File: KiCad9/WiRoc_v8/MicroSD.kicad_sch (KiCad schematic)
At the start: 13 parts, among them J3 Micro_SD_Card_Det1

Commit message: etc
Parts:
- J3: LCSC Part # (none) -> C2962372; Manufacturer (none) -> Hanbo Electronic; ManufacturerPartNumber (none) -> TF-018B-H15
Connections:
- net SDC0-CLK-2: now reaches J3.5 (CLK), R22.2, RV6.1
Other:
- moved on the sheet: R22
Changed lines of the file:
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@@
 	(wire
 		(pts
-			(xy 58.42 71.12) (xy 63.5 71.12)
+			(xy 53.34 71.12) (xy 60.96 71.12)
 		)
 		(stroke
@@
 	(wire
 		(pts
-			(xy 71.12 71.12) (xy 93.98 71.12)
+			(xy 68.58 71.12) (xy 93.98 71.12)
 		)
 		(stroke
@@
 			(width 0)
 			(type default)
+		)
+	)
+	(label "SDC0-CLK-2"
+		(at 90.17 71.12 0)
+		(effects
+			(font
+				(size 1.524 1.524)
+			)
+			(justify left bottom)
 		)
 	)
@@
 	(global_label "SDC0-CLK"
 		(shape input)
-		(at 58.42 71.12 180)
+		(at 53.34 71.12 180)
 		(fields_autoplaced yes)
 		(effects
@@
 		)
 		(property "Intersheetrefs" "${INTERSHEET_REFS}"
-			(at 43.5038 71.12 0)
+			(at 38.4238 71.12 0)
 			(effects
 				(font
@@
 				(justify right)
 				(hide yes)
+			)
+		)
+	)
+	(rule_area
+		(polyline
+			(pts
+				(xy 69.85 58.42) (xy 69.85 86.36) (xy 72.39 86.36) (xy 72.39 58.42)
+			)
+			(stroke
+				(width 0)
+				(type dash)
+			)
+			(fill
+				(type none)
+			)
+		)
+	)
+	(netclass_flag ""
+		(length 2.54)
+		(shape round)
+		(at 55.88 71.12 0)
+		(fields_autoplaced yes)
+		(effects
+			(font
+				(size 1.524 1.524)
+			)
+			(justify left bottom)
+		)
+		(property "Netclass" "SD-CARD-LINES"
+			(at 56.5099 68.58 0)
+			(effects
+				(font
+					(size 1.27 1.27)
+				)
+				(justify left)
+			)
+		)
+		(property "Component Class" ""
+			(at -130.81 35.56 0)
+			(effects
+				(font
+					(size 1.27 1.27)
+					(italic yes)
+				)
+			)
+		)
+	)
+	(netclass_flag ""
+		(length 2.54)
+		(shape round)
+		(at 71.12 58.42 0)
+		(fields_autoplaced yes)
+		(effects
+			(font
+				(size 1.524 1.524)
+			)
+			(justify left bottom)
+		)
+		(property "Netclass" "SD-CARD-LINES"
+			(at 71.7499 55.88 0)
+			(effects
+				(font
+					(size 1.27 1.27)
+				)
+				(justify left)
+			)
+		)
+		(property "Component Class" ""
+			(at -115.57 22.86 0)
+			(effects
+				(font
+					(size 1.27 1.27)
+					(italic yes)
+				)
 			)
 		)
@@
 			)
 		)
+		(property "LCSC Part #" "C2962372"
+			(at 148.59 71.12 0)
+			(effects
+				(font
+					(size 1.27 1.27)
+				)
+				(hide yes)
+			)
+		)
+		(property "Manufacturer" "Hanbo Electronic"
+			(at 148.59 71.12 0)
+			(effects
+				(font
+					(size 1.27 1.27)
+				)
+				(hide yes)
+			)
+		)
+		(property "ManufacturerPartNumber" "TF-018B-H15"
+			(at 148.59 71.12 0)
+			(effects
+				(font
+					(size 1.27 1.27)
+				)
+				(hide yes)
+			)
+		)
 		(pin "7"
 		)
@@
 	(symbol
 		(lib_id "Device:R")
-		(at 67.31 71.12 90)
+		(at 64.77 71.12 90)
 		(unit 1)
 		(exclude_from_sim no)
@@
 		(dnp no)
 		(property "Reference" "R22"
-			(at 72.39 73.66 90)
+			(at 69.85 73.66 90)
 			(effects
 				(font
@@
 		)
 		(property "Value" "33R"
-			(at 63.5 73.66 90)
+			(at 60.96 73.66 90)
 			(effects
 				(font
@@
 		)
 		(property "Footprint" "Resistor_SMD:R_0402_1005Metric"
-			(at 67.31 72.898 90)
+			(at 64.77 72.898 90)
 			(effects
 				(font
@@
 		)
 		(property "Datasheet" "~"
-			(at 67.31 71.12 0)
+			(at 64.77 71.12 0)
 			(effects
 				(font
@@
 		)
 		(property "Description" ""
-			(at 67.31 71.12 0)
-			(effects
-				(font
+			(at 64.77 71.12 0)
+			(effects
+				(font

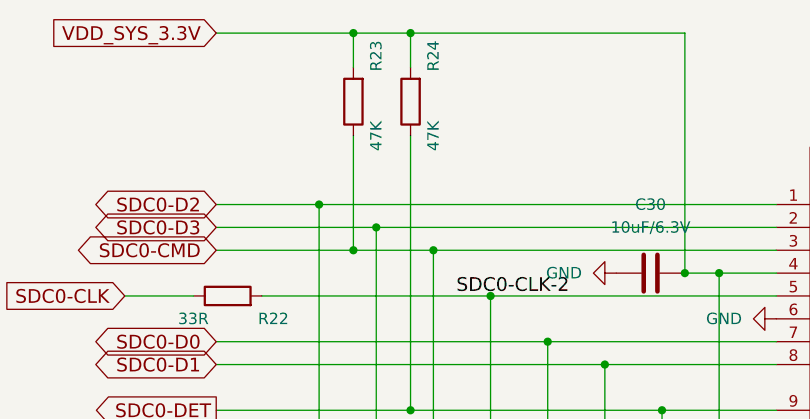
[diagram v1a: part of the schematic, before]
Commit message: add bom
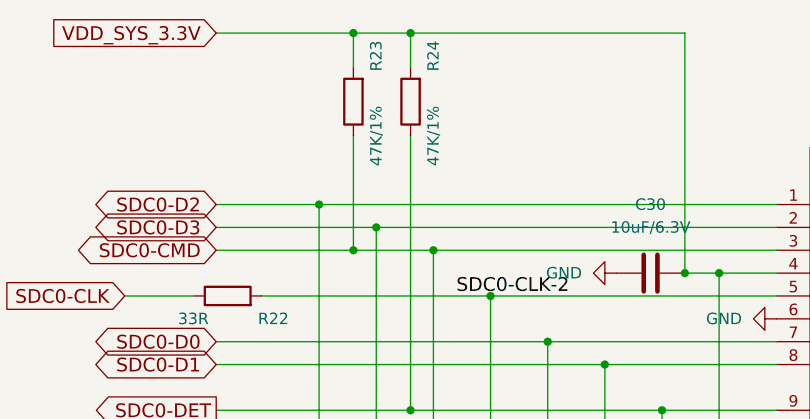
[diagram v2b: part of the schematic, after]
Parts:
- C30: IncludeInBOM (none) -> TRUE; JLCBasicExtended (none) -> Basic; LCSC Part # (none) -> C15525; Manufacturer (none) -> Samsung Electro-Mechanics; ManufacturerPartNumber (none) -> CL05A106MQ5NUNC; Package (none) -> 0402
- J3: IncludeInBOM (none) -> TRUE; JLCBasicExtended (none) -> Extended
- R22: IncludeInBOM (none) -> TRUE; JLCBasicExtended (none) -> Basic; LCSC Part # (none) -> C25105; Manufacturer (none) -> Uniroyal Elec; ManufacturerPartNumber (none) -> 0402WGF330JTCE; Package (none) -> 0402
- R23, R24: value 47K -> 47K/1%; IncludeInBOM (none) -> TRUE; JLCBasicExtended (none) -> Basic; LCSC Part # (none) -> C25792; Manufacturer (none) -> Uniroyal Elec; ManufacturerPartNumber (none) -> 0402WGF4702TCE; Package (none) -> 0402
- RV1, RV2, RV3, RV4, RV5, RV6, RV7, RV8: IncludeInBOM (none) -> TRUE; JLCBasicExtended (none) -> Extended; LCSC Part # (none) -> C92016; Manufacturer (none) -> TDK; ManufacturerPartNumber (none) -> AVRL101A1R1NTB; Package (none) -> 0402

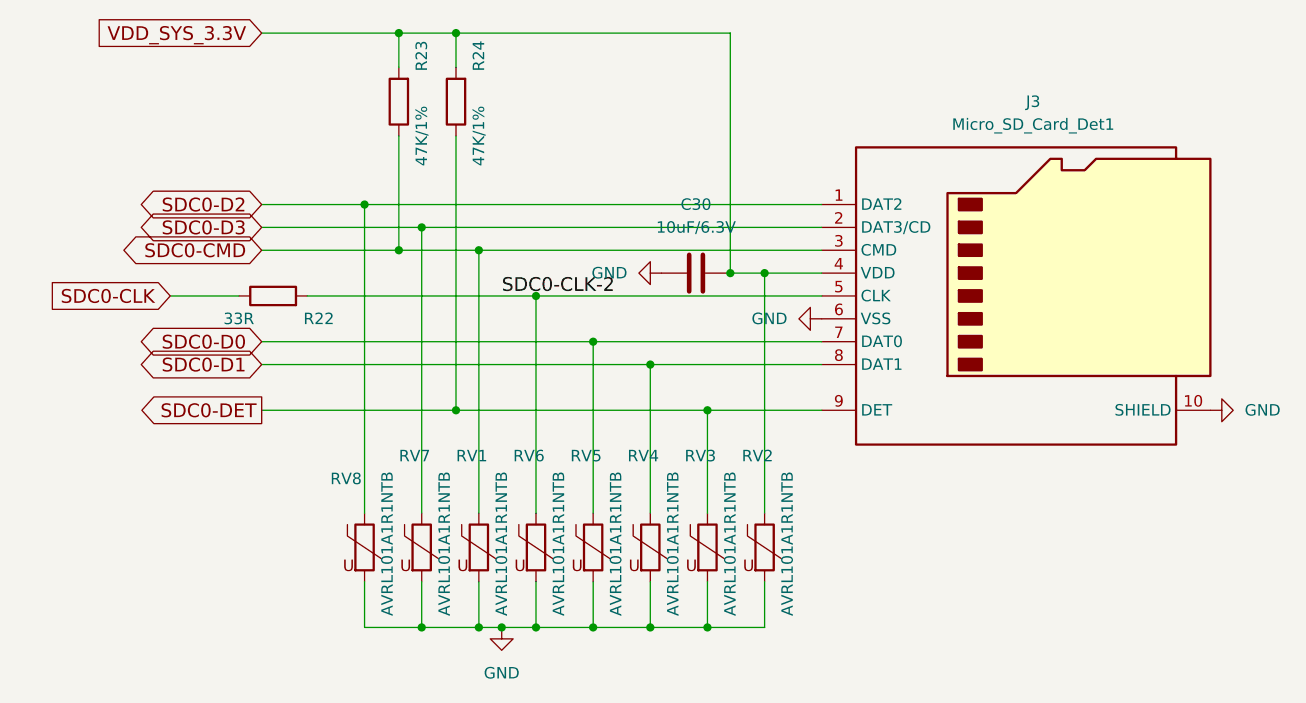
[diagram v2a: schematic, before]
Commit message: change to 10uF in pdn, vdd-dram area to south caps, remove varistor, etc
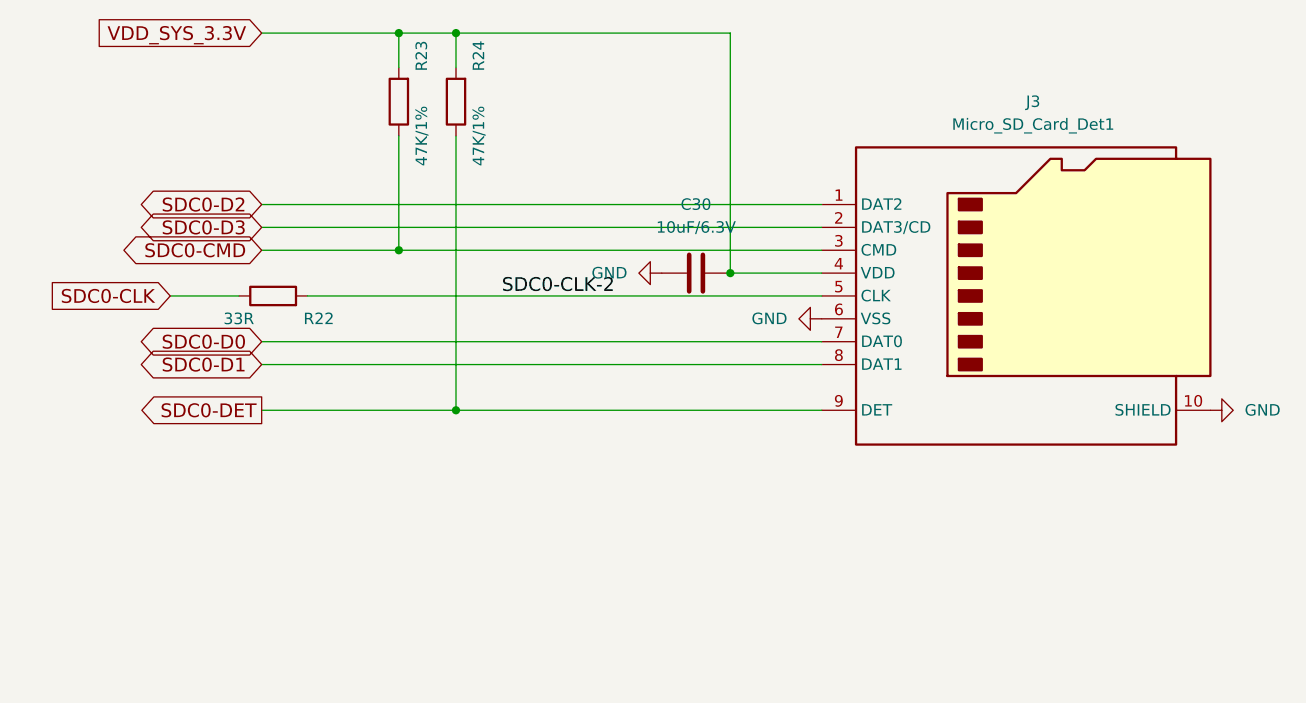
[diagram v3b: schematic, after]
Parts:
- removed RV1, RV2, RV3, RV4, RV5, RV6, RV7, RV8: AVRL101A1R1NTB, Resistor_SMD:R_0402_1005Metric, symbol Device:Varistor

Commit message: many small changes, change eMMC
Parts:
- R22: value 33R -> 22R
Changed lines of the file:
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@@
 			)
 		)
-		(property "Value" "33R"
-			(at 60.96 73.66 90)
+		(property "Value" "22R"
+			(at 64.77 71.374 90)
 			(effects
 				(font

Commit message: etc
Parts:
- R22: LCSC Part # C25105 -> C25092; ManufacturerPartNumber 0402WGF330JTCE -> 0402WGF220JTCE
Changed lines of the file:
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@@
 			)
 		)
-		(property "LCSC Part #" "C25105"
+		(property "LCSC Part #" "C25092"
 			(at 64.77 71.12 90)
 			(effects
@@
 			)
 		)
-		(property "ManufacturerPartNumber" "0402WGF330JTCE"
+		(property "ManufacturerPartNumber" "0402WGF220JTCE"
 			(at 64.77 71.12 90)
 			(effects

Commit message: add ethernet etc
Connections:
- net GND: now also R24.1
- net SDC0-DET: now also R24.2; no longer J3.9 (DET), R24.1
- net VDD_SYS_3.3V: no longer R24.2
- no-connect marks 0 -> 1
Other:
- moved on the sheet: R24
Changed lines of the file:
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@@
-	)
-	(junction
-		(at 85.09 41.91)
-		(diameter 0)
-		(color 0 0 0 0)
-	)
-	(junction
-		(at 85.09 83.82)
-		(diameter 0)
-		(color 0 0 0 0)
 	)
 	(junction
@@
 		(color 0 0 0 0)
 	)
+	(no_connect
+		(at 125.73 83.82)
+	)
 	(wire
 		(pts
@@
 	(wire
 		(pts
-			(xy 85.09 41.91) (xy 115.57 41.91)
-		)
-		(stroke
-			(width 0)
-			(type default)
-		)
-	)
-	(wire
-		(pts
 			(xy 63.5 41.91) (xy 78.74 41.91)
 		)
@@
 	(wire
 		(pts
-			(xy 85.09 53.34) (xy 85.09 83.82)
-		)
-		(stroke
-			(width 0)
-			(type default)
-		)
-	)
-	(wire
-		(pts
-			(xy 85.09 83.82) (xy 125.73 83.82)
-		)
-		(stroke
-			(width 0)
-			(type default)
-		)
-	)
-	(wire
-		(pts
-			(xy 78.74 41.91) (xy 85.09 41.91)
+			(xy 78.74 41.91) (xy 115.57 41.91)
 		)
 		(stroke
@@
 	(wire
 		(pts
-			(xy 85.09 41.91) (xy 85.09 45.72)
-		)
-		(stroke
-			(width 0)
-			(type default)
-		)
-	)
-	(wire
-		(pts
 			(xy 63.5 78.74) (xy 125.73 78.74)
 		)
@@
 	(wire
 		(pts
-			(xy 63.5 83.82) (xy 85.09 83.82)
+			(xy 63.5 83.82) (xy 88.9 83.82)
+		)
+		(stroke
+			(width 0)
+			(type default)
+		)
+	)
+	(wire
+		(pts
+			(xy 88.9 87.63) (xy 88.9 83.82)
 		)
 		(stroke
@@
 		(polyline
 			(pts
-				(xy 69.85 58.42) (xy 69.85 86.36) (xy 72.39 86.36) (xy 72.39 58.42)
+				(xy 69.85 58.42) (xy 69.85 81.28) (xy 72.39 81.28) (xy 72.39 58.42)
 			)
 			(stroke
@@
 	(symbol
 		(lib_id "Device:R")
-		(at 85.09 49.53 180)
+		(at 88.9 91.44 180)
 		(unit 1)
 		(exclude_from_sim no)
@@
 		(dnp no)
 		(property "Reference" "R24"
-			(at 87.63 44.45 90)
+			(at 91.44 86.36 90)
 			(effects
 				(font
@@
 		)
 		(property "Value" "47K/1%"
-			(at 87.63 53.34 90)
+			(at 91.44 95.25 90)
 			(effects
 				(font
@@
 		)
 		(property "Footprint" "Resistor_SMD:R_0402_1005Metric"
-			(at 86.868 49.53 90)
+			(at 90.678 91.44 90)
 			(effects
 				(font
@@
 		)
 		(property "Datasheet" "~"
-			(at 85.09 49.53 0)
+			(at 88.9 91.44 0)
 			(effects
 				(font
@@
 		)
 		(property "Description" ""
-			(at 85.09 49.53 0)
+			(at 88.9 91.44 0)
 			(effects
 				(font
@@
 		)
 		(property "JLCBasicExtended" "Basic"
-			(at 85.09 49.53 90)
+			(at 88.9 91.44 90)
 			(effects
 				(font
@@
 		)
 		(property "IncludeInBOM" "TRUE"
-			(at 85.09 49.53 90)
+			(at 88.9 91.44 90)
 			(effects
 				(font
@@
 		)
 		(property "LCSC Part #" "C25792"
-			(at 85.09 49.53 90)
+			(at 88.9 91.44 90)
 			(effects
 				(font
@@
 		)
 		(property "Manufacturer" "Uniroyal Elec"
-			(at 85.09 49.53 90)
+			(at 88.9 91.44 90)
 			(effects
 				(font
@@
 		)
 		(property "ManufacturerPartNumber" "0402WGF4702TCE"
-			(at 85.09 49.53 90)
+			(at 88.9 91.44 90)
 			(effects
 				(font
@@
 		)
 		(property "Package" "0402"
-			(at 85.09 49.53 90)
+			(at 88.9 91.44 90)
 			(effects
 				(font
@@
 					(unit 1)
 				)
+			)
+		)
+	)
+	(symbol
+		(lib_id "power:GND")
+		(at 88.9 95.25 0)
+		(unit 1)
+		(exclude_from_sim no)
+		(in_bom yes)
+		(on_board yes)
+		(dnp no)
+		(fields_autoplaced yes)
+		(property "Reference" "#PWR0117"
+			(at 88.9 101.6 0)
+			(effects
+				(font
+					(size 1.27 1.27)
+				)
+				(hide yes)
+			)
+		)
+		(property "Value" "GND"
+			(at 88.9 100.33 0)
+			(effects
+				(font
+					(size 1.27 1.27)
+				)
+			)
+		)
+		(property "Footprint" ""
+			(at 88.9 95.25 0)
+			(effects
+				(font
+					(size 1.27 1.27)
+				)
+				(hide yes)
+			)
+		)
+		(property "Datasheet" ""
+			(at 88.9 95.25 0)
+			(effects
+				(font
+					(size 1.27 1.27)
+				)
+				(hide yes)
+			)
+		)
+		(property "Description" ""
+			(at 88.9 95.25 0)
+			(effects
+				(font
+					(size 1.27 1.27)
+				)
+				(hide yes)
+			)
+		)
+		(pin "1"
+		)
+		(instances
+			(project "WiRoc_NanoPi"
+				(path "/8ba0b499-eaca-4cd5-a002-c6bdb610cc8c/d4d2b4ff-c69b-4368-8319-409c337f9058"
+					(reference "#PWR0117")
+					(unit 1)
+				)
